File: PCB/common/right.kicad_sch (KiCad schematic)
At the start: 89 parts, among them J2 TRS

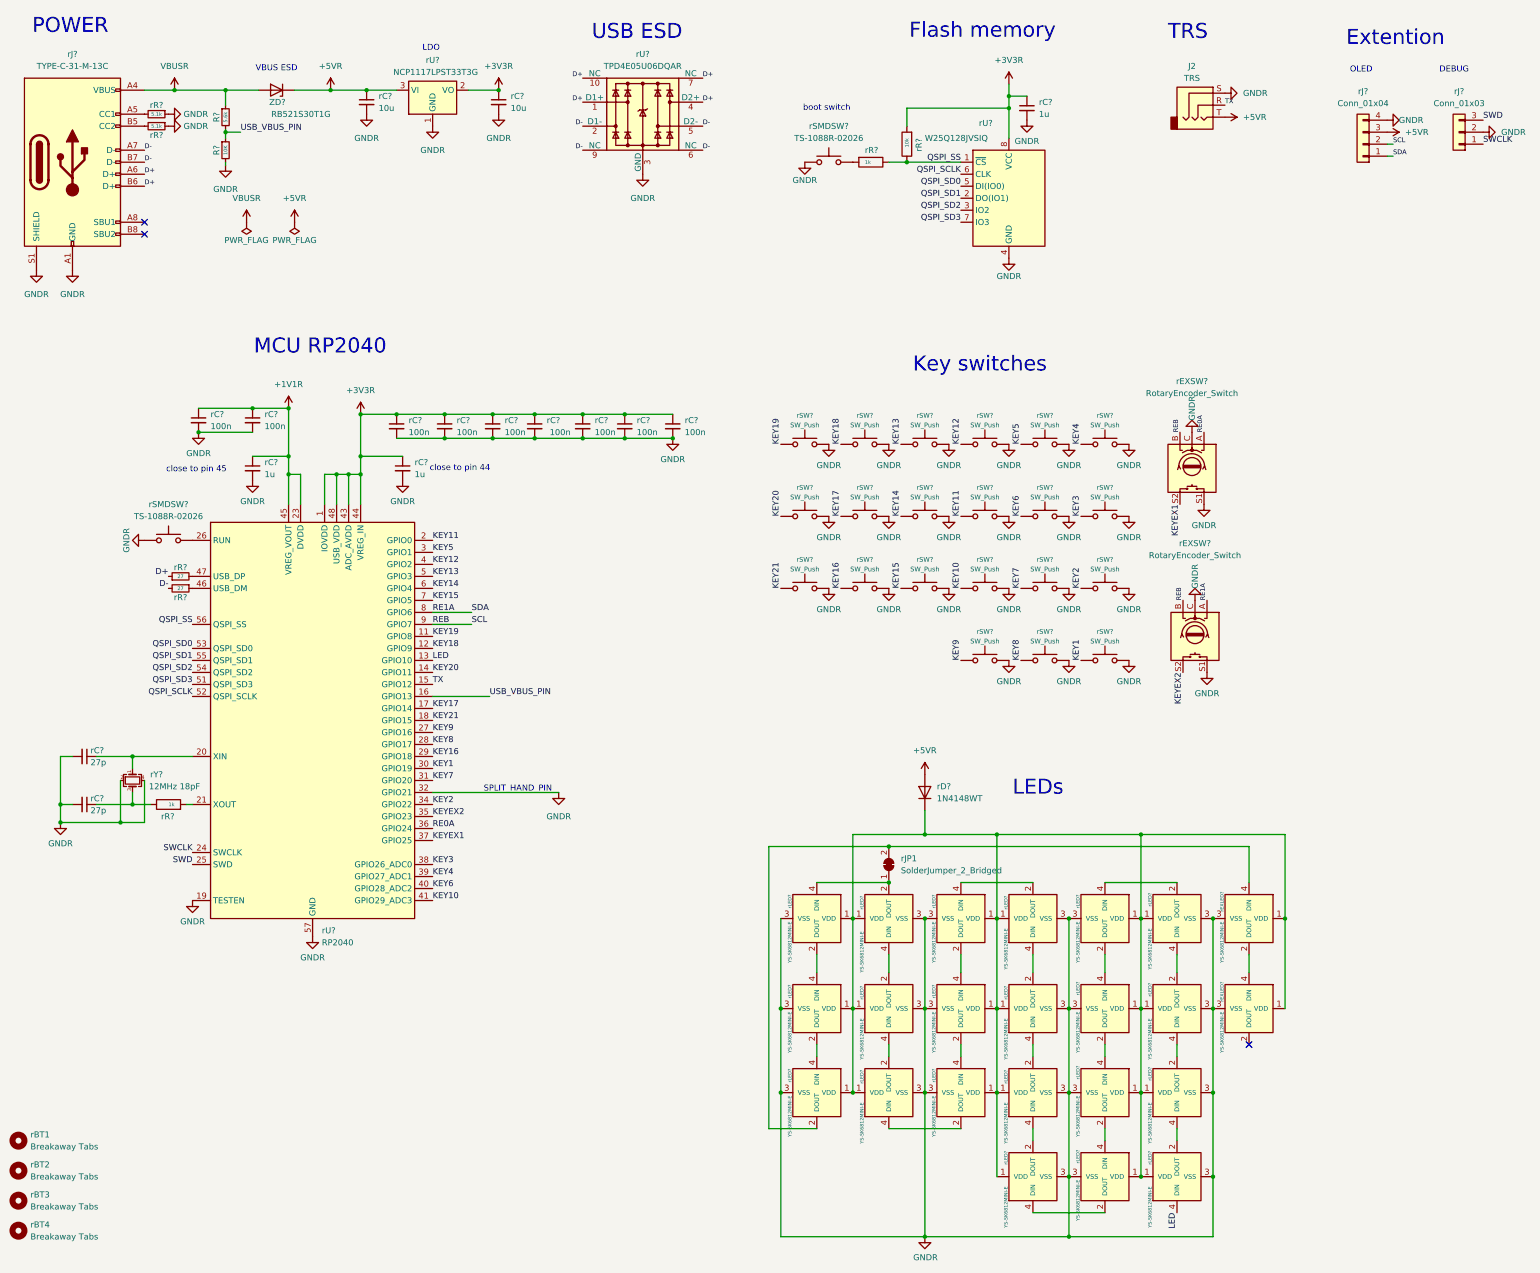
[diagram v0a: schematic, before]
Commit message: Removed unused electronics
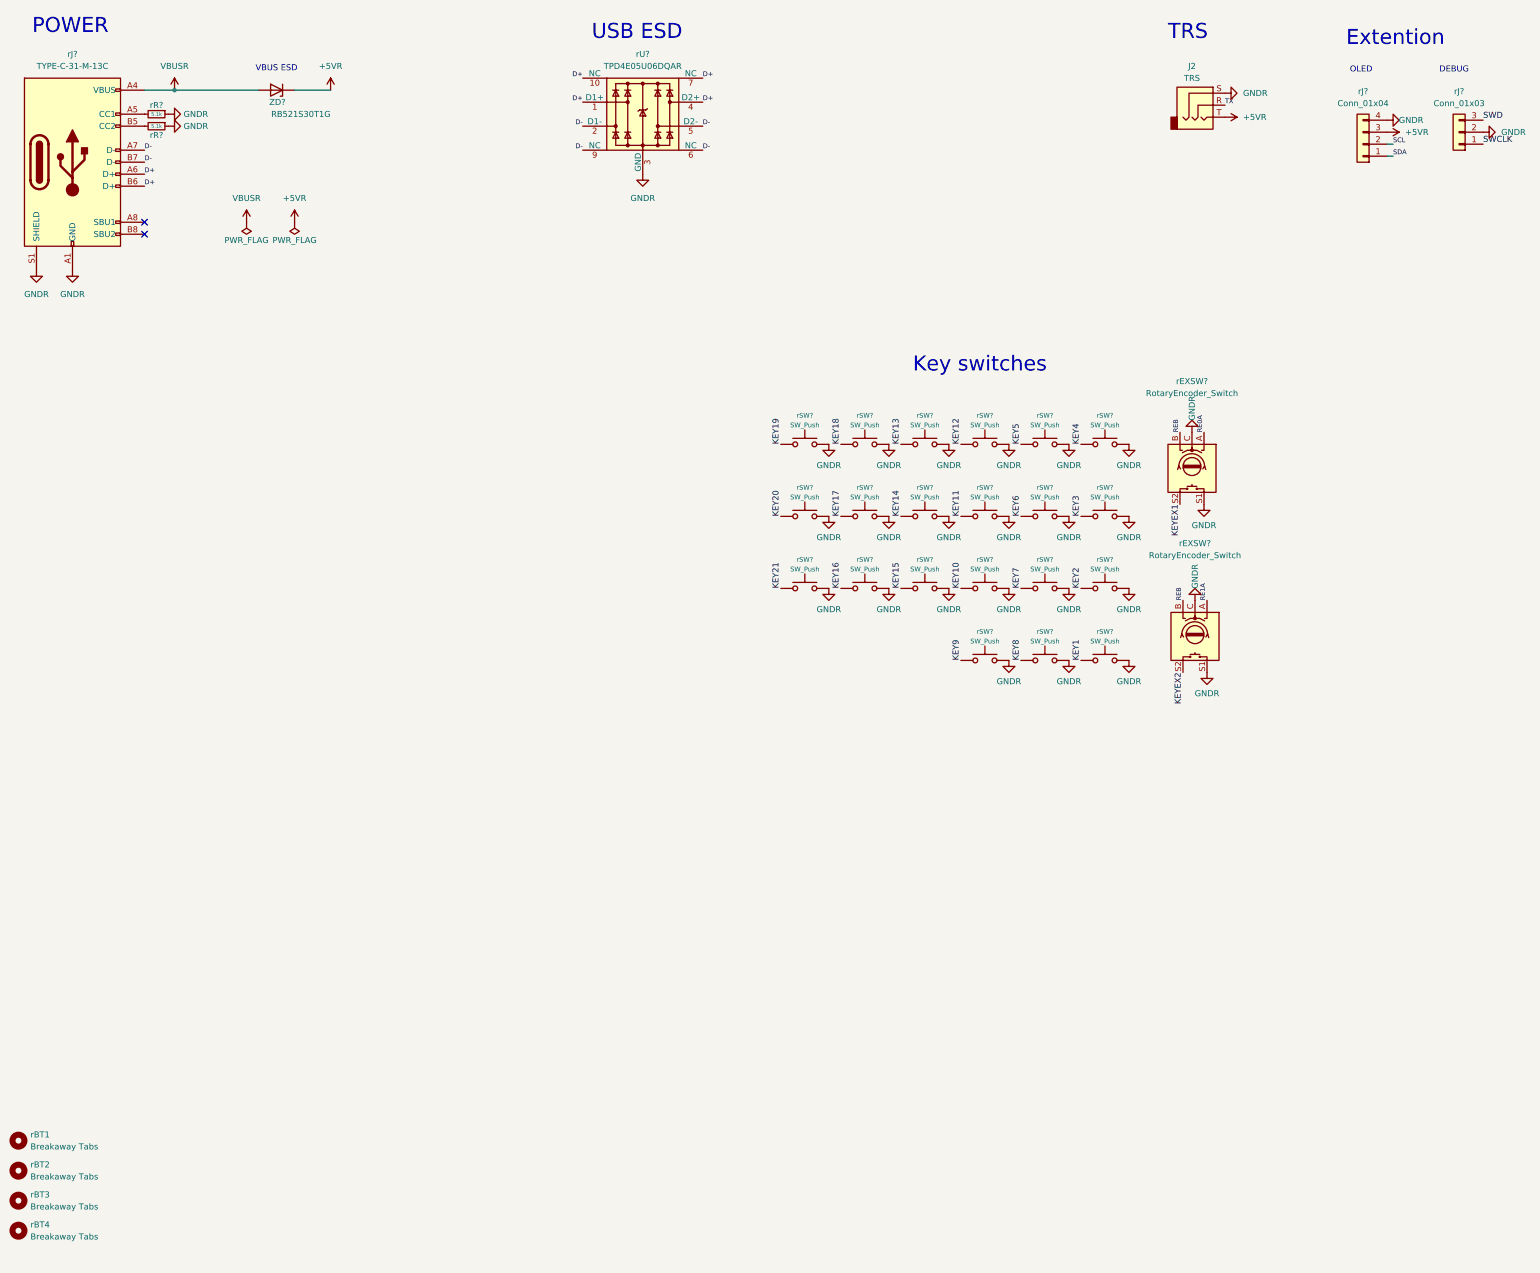
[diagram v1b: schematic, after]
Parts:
- removed R?: 5.6k, Resistor_SMD:R_0402_1005Metric, symbol Device:R_Small
- removed R?: 10K, Resistor_SMD:R_0402_1005Metric, symbol Device:R_Small
- removed rC? (x2): 27p, Capacitor_SMD:C_0402_1005Metric, symbol Device:C_Small
- removed rC? (x9): 100n, Capacitor_SMD:C_0402_1005Metric, symbol Device:C_Small
- removed rC? (x3): 1u, Capacitor_SMD:C_0402_1005Metric, symbol Device:C_Small
- removed rC? (x2): 10u, Capacitor_SMD:C_0402_1005Metric, symbol Device:C_Small
- removed rD?: 1N4148WT, Diode_SMD:D_SOD-523, symbol Diode:1N4148WT
- removed rEXLED? (x2), rLED? (x21): YS-SK6812MINI-E, kbd_local:YS-SK6812MINI-E, symbol kbd_local:YS-SK6812MINI-E
- removed rJP1: SolderJumper_2_Bridged, Jumper:SolderJumper-2_P1.3mm_Open_RoundedPad1.0x1.5mm, symbol Jumper:SolderJumper_2_Bridged
- removed rR? (x2): 1k, Resistor_SMD:R_0402_1005Metric, symbol Device:R
- removed rR?: 10k, Resistor_SMD:R_0402_1005Metric, symbol Device:R
- removed rR? (x2): 27, Resistor_SMD:R_0402_1005Metric, symbol Device:R_Small
- removed rSMDSW? (x2): TS-1088R-02026, kbd_local:TS-1088R-02026, symbol Switch:SW_Push
- removed rU?: NCP1117LPST33T3G, Package_TO_SOT_SMD:SOT-223-3_TabPin2, symbol Regulator_Linear:NCP1117-3.3_SOT223
- removed rU?: W25Q128JVSIQ, Package_SO:SOIC-8_5.23x5.23mm_P1.27mm, symbol Memory_Flash:W25Q128JVS
- removed rU?: RP2040, Package_DFN_QFN:QFN-56-1EP_7x7mm_P0.4mm_EP3.2x3.2mm, symbol MCU_RaspberryPi:RP2040
- removed rY?: 12MHz 18pF, Crystal:Crystal_SMD_3225-4Pin_3.2x2.5mm, symbol Device:Crystal_GND24_Small
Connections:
- net RE1A: no longer rJ?.1 (Pin_1)
- net REB: no longer rJ?.2 (Pin_2)
- new net SCL: rJ?.2 (Pin_2)
- new net SDA: rJ?.1 (Pin_1)
- no-connect marks 3 -> 2
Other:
- note removed: "Flash memory"
- note removed: "LDO"
- note removed: "LEDs"
- note removed: "MCU RP2040"
- note removed: "SPLIT_HAND_PIN"
- note removed: "boot switch"
- note removed: "close to pin 44"
- note removed: "close to pin 45"
